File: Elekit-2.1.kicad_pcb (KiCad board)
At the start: 2 copper layers, 77.5 x 77.5 mm, 114 parts, among them J101 Conn_01x03_Male, J102 Conn_01x03_Male, J103 Screw_Terminal_01x02, J104 Conn_01x03_Male, J105 Conn_01x01_Pin, J106 Conn_01x01_Pin, J107 Conn_01x01_Pin, J108 Conn_01x01_Pin, J111 Conn_01x01_Pin, J112 Conn_01x01_Pin, J113 Conn_01x01_Pin, J117 Conn_01x01_Pin, J118 Conn_01x01_Pin, J119 Conn_01x01_Pin, J120 Conn_01x01_Pin, J121 Conn_01x01_Pin, J122 Conn_01x01_Pin, J2 Screw_Terminal_01x02, J3 Screw_Terminal_01x02, J4 Screw_Terminal_01x02, J5 Conn_01x03_Male, J6 Conn_01x06_Male, J9 Conn_01x03_Male, Q1 2N7002, Q101 2N7002, Q3 2N7002, U1 MINI_5PTP, U10 TS-1187A-B-A-B, U101 DRV8876PWPR, U102 DRV8876PWPR, U103 LSM303AGRTR, U104 DRV8876PWPR, U106 TS-1187A-B-A-B, U107 R-78E5.0-0.5, U5 SRV05-4-P-T7, U7 ME6211C33M5G-N, U8 TS-1187A-B-A-B, U9 ESP32-C3-WROOM-02-N4(4MB)

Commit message: add jst ph connector for lidar
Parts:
- added J109: Conn_01x04_Socket, Connector_JST:JST_PH_S4B-PH-K_1x04_P2.00mm_Horizontal, F.Cu at (52.0, 73.0)
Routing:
- net /TX: track 21.5 -> 78.1 mm, vias 1 -> 3
- net /RX: track 18.1 -> 71.6 mm, vias 1 -> 3
- net /JoyY: track 80.1 -> 57.1 mm
- net +5V: track 211.5 -> 233.0 mm
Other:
- board text added: "+5V"
- board text added: "PWM"

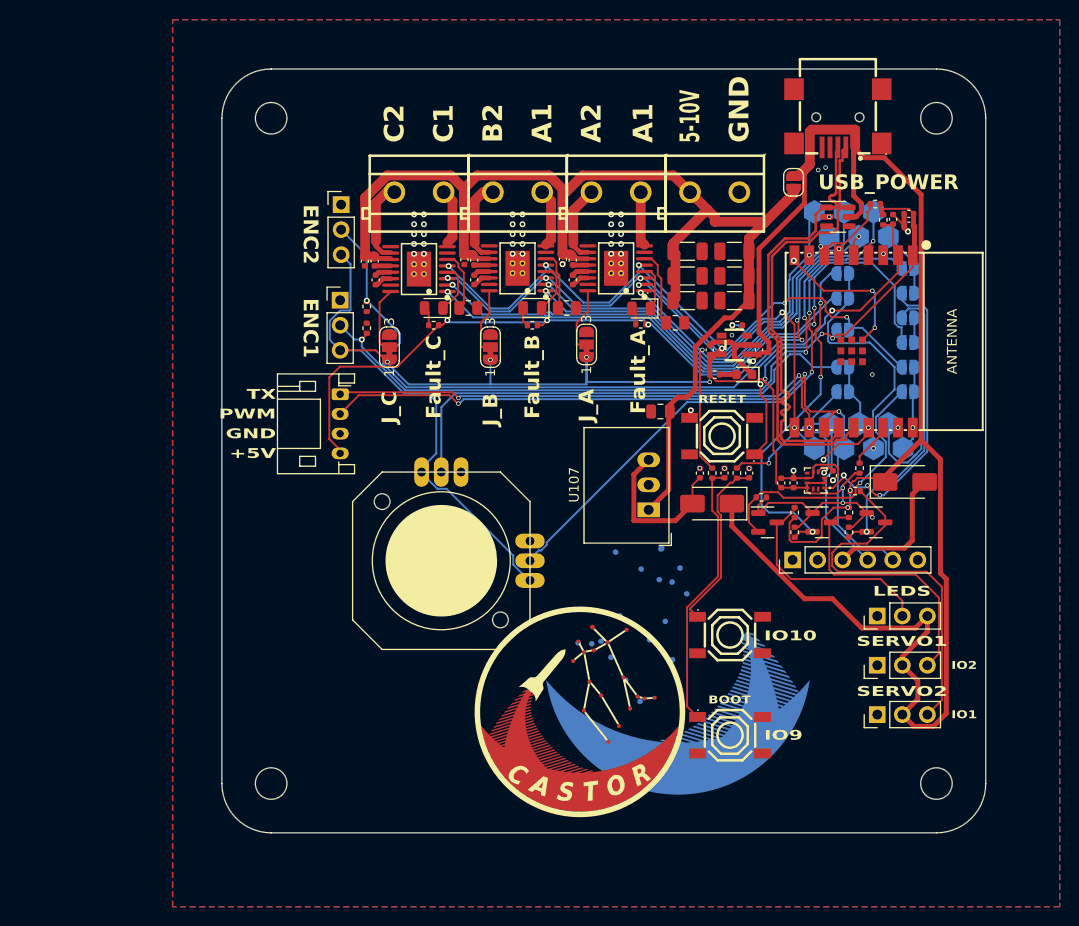
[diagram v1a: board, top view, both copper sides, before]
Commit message: add bno085
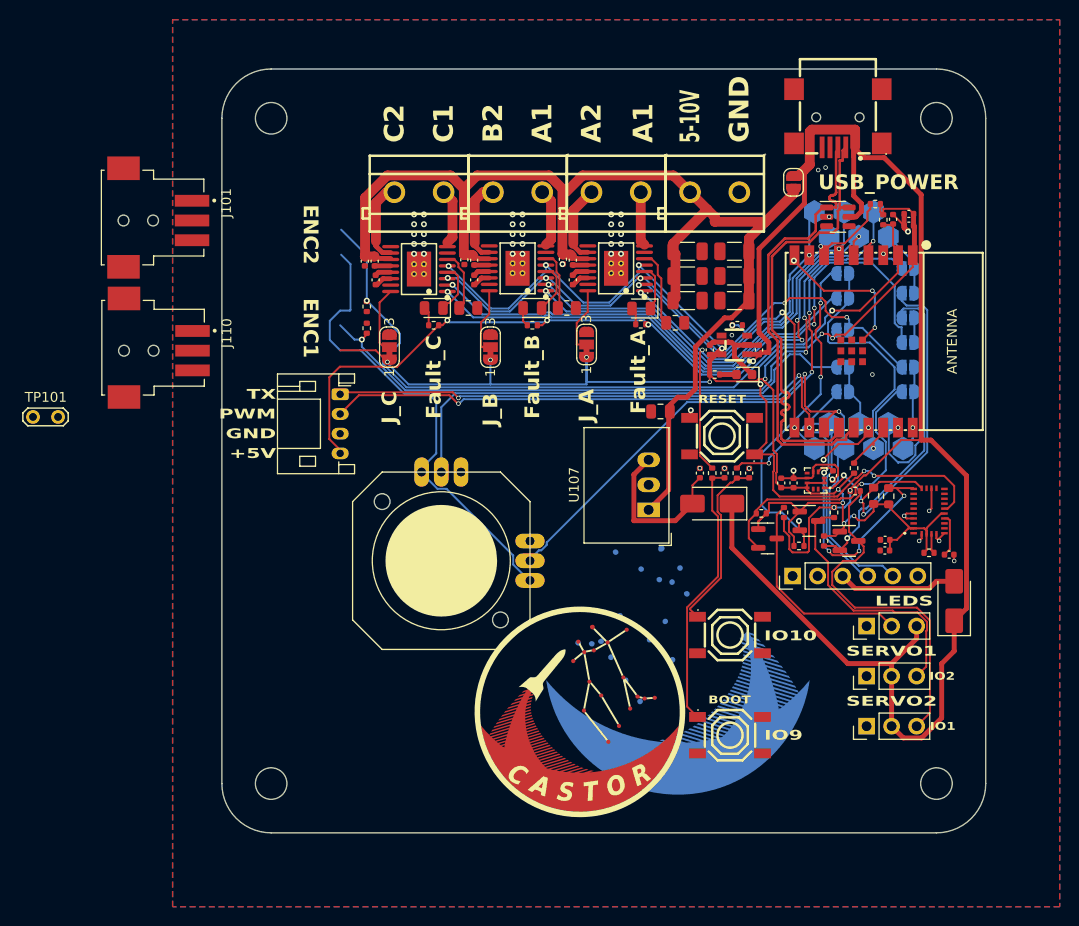
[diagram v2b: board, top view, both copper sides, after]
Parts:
- removed J102: Conn_01x03_Male, Connector_PinHeader_2.54mm:PinHeader_1x03_P2.54mm_Vertical
- added C126: 100n 16V, Capacitor_SMD:C_0402_1005Metric, F.Cu at (107.3, 87.8)
- added C127: 100n 16V, Capacitor_SMD:C_0402_1005Metric, F.Cu at (107.3, 88.9)
- added C128: 100n 16V, Capacitor_SMD:C_0402_1005Metric, F.Cu at (113.8, 89.3)
- added IC101: BNO085, KiCad:BNO085, F.Cu at (111.7, 84.9)
- added J110: Conn_01x03_Socket, SnapEDA Library:TE_292173-3, F.Cu at (33.0, 68.6)
- added R122: 3k9, Resistor_SMD:R_0603_1608Metric, F.Cu at (106.1, 83.3)
- added R123: 3k9, Resistor_SMD:R_0603_1608Metric, F.Cu at (107.7, 83.3)
- added R124: 10k, Resistor_SMD:R_0402_1005Metric, F.Cu at (111.7, 89.1)
- added TP101: TestPoint_2Pole, TestPoint:TestPoint_2Pads_Pitch2.54mm_Drill0.8mm, F.Cu at (20.8, 75.3)
- J101: value Conn_01x03_Male -> Conn_01x03_Socket; footprint Connector_PinHeader_2.54mm:PinHeader_1x03_P2.54mm_Vertical -> SnapEDA Library:TE_292173-3
- moved J101 20.7 mm to (33.0, 55.4), turned to -90 degrees
- moved D8 13.1 mm to (114.3, 94.0), turned to 90 degrees
- moved Q1 3.32 mm to (103.6, 87.9)
- moved R113 2.67 mm to (101.1, 87.9)
- moved R109 1.63 mm to (94.7, 85.1)
- moved J6 1.63 mm to (97.9, 91.4)
- moved Q101 1.63 mm to (95.4, 87.6)
- moved J5 1.61 mm to (105.4, 106.7)
- moved J9 1.55 mm to (105.4, 101.6)
- moved R111 1.51 mm to (102.1, 85.0)
- moved J104 1.49 mm to (105.4, 96.5)
- moved R112 1.46 mm to (98.6, 88.4), turned to 0 degrees
- moved Q3 1.31 mm to (99.6, 85.9)
- moved R110 1.09 mm to (97.0, 85.0)
- moved R108 0.56 mm to (104.1, 80.5)
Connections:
- J101 pad 1: GND -> +3.3V
- J101 pad 3: +3.3V -> GND
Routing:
- net /CHIP_PU: track 34.2 -> 63.0 mm, vias 2 -> 4
- net /SDA: track 11.7 -> 35.2 mm, vias 1 -> 4
- net +3.3V: track 224.7 -> 245.7 mm, vias 14 -> 15
- net /SCL: track 32.1 -> 41.9 mm
- net GND: track 39.4 -> 47.3 mm, vias 46 -> 51
- net Net-(IC101-CAP): track 0.00 -> 4.34 mm
- net /SERVO1: track 38.0 -> 35.4 mm
- net /SERVO1_C: track 30.3 -> 32.9 mm
- net /TX: track 78.1 -> 80.6 mm
- net +5V: track 233.0 -> 235.4 mm
- net Net-(D8-A): track 14.3 -> 12.1 mm
- net Net-(IC101-BOOTN): track 0.00 -> 2.03 mm
- net /RX: track 71.6 -> 73.4 mm
- net /LED_in: track 28.0 -> 29.4 mm
- net /LED_out: track 22.7 -> 21.6 mm
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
